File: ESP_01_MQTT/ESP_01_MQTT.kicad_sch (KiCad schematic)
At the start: 33 parts, among them J1 Conn_01x01, J2 Conn_01x01, J3 Conn_01x01, J4 Conn_01x01, J5 Conn_01x01, J6 Conn_01x01_Pin, J7 Conn_01x06, J8 Conn_01x05, M1 LM2596-StepDownModul, Q1 BC817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

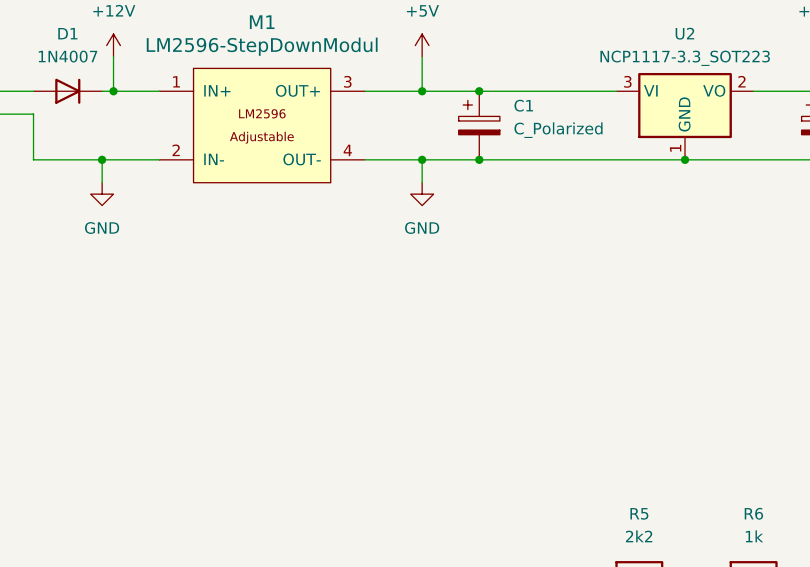
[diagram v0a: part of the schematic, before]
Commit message: Hardware gelötet
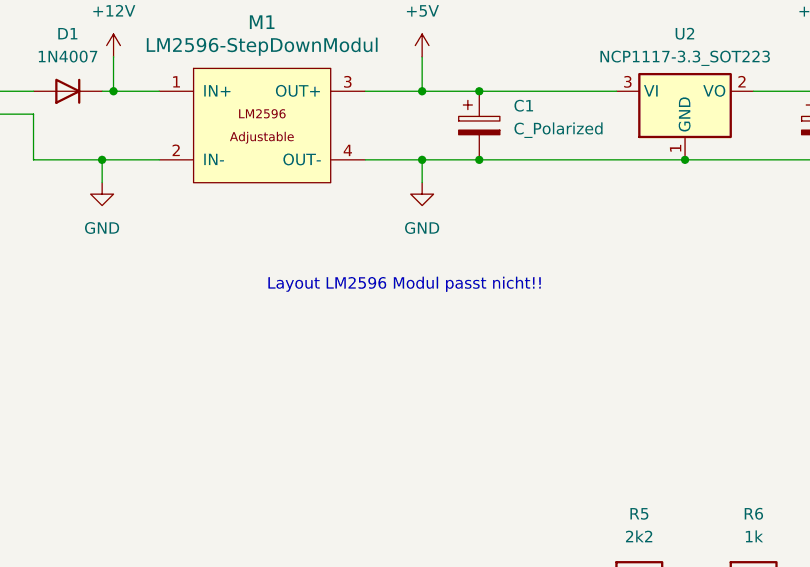
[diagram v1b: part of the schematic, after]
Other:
- note added: "Layout LM2596 Modul passt nicht!!"
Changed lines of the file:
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@@
+		)
+	)
+	(text "Layout LM2596 Modul passt nicht!!"
+		(exclude_from_sim no)
+		(at 80.645 53.34 0)
+		(effects
+			(font
+				(size 1.27 1.27)
+			)
 		)
 	)
